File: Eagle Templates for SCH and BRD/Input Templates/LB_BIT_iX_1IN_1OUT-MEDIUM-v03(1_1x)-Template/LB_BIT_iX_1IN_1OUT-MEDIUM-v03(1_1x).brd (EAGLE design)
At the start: 21.4 x 18.2 mm, 17 parts, among them U1 LV321SOT23-5, U2 LV321SOT23-5

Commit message: added bitlab logo and made minor changes to board templates. Updated littlebits library.
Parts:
- added U$5: (no value), LITTLEBITS:BITLAB-LOGO
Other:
- board text added: "iX Name Here"
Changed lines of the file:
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@@
 <layer number="113" name="extra" color="10" fill="1" visible="yes" active="yes"/>
 <layer number="116" name="Patch_BOT" color="9" fill="4" visible="yes" active="yes"/>
+<layer number="118" name="Rect_Pads" color="7" fill="1" visible="no" active="yes"/>
 <layer number="121" name="_tsilk" color="7" fill="1" visible="yes" active="yes"/>
 <layer number="122" name="_bsilk" color="7" fill="1" visible="yes" active="yes"/>
@@
 <wire x1="3.305" y1="22.31" x2="2.51" y2="22.31" width="1" layer="46"/>
 <wire x1="2.51" y1="22.31" x2="2.51" y2="4.11" width="1" layer="46"/>
+<text x="21.6" y="13.21" size="1.3" layer="21" font="vector" rot="SR270" align="center">iX Name Here</text>
 </plain>
 <attributes>
@@
 <element name="U$1" library="LITTLEBITS" package="FABDWG01-OHW" value="FRAME-LETTER" x="0" y="0"/>
 <element name="U$4" library="ohw-logo" package="OSHW_FILLX150_NOTEXT" value="" x="19" y="16.9" rot="MR90"/>
+<element name="U$5" library="LITTLEBITS" package="BITLAB-LOGO" value="" x="19.5" y="15" rot="R270"/>
 </elements>
 <signals>

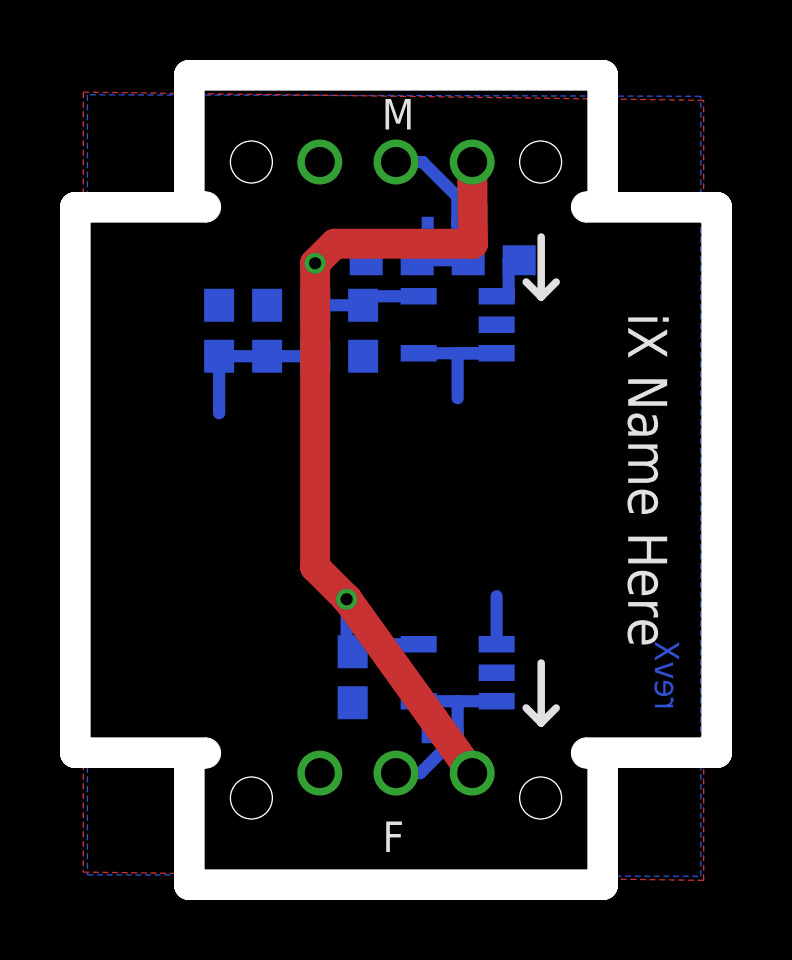
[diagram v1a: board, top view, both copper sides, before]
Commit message: Updated templates
- Added ferrite beads
- Moved text and annotations off of Nets layer
- Minor layout changes
- Removed I/O/W prefix from reference designators
- Removed output stage components from output bits
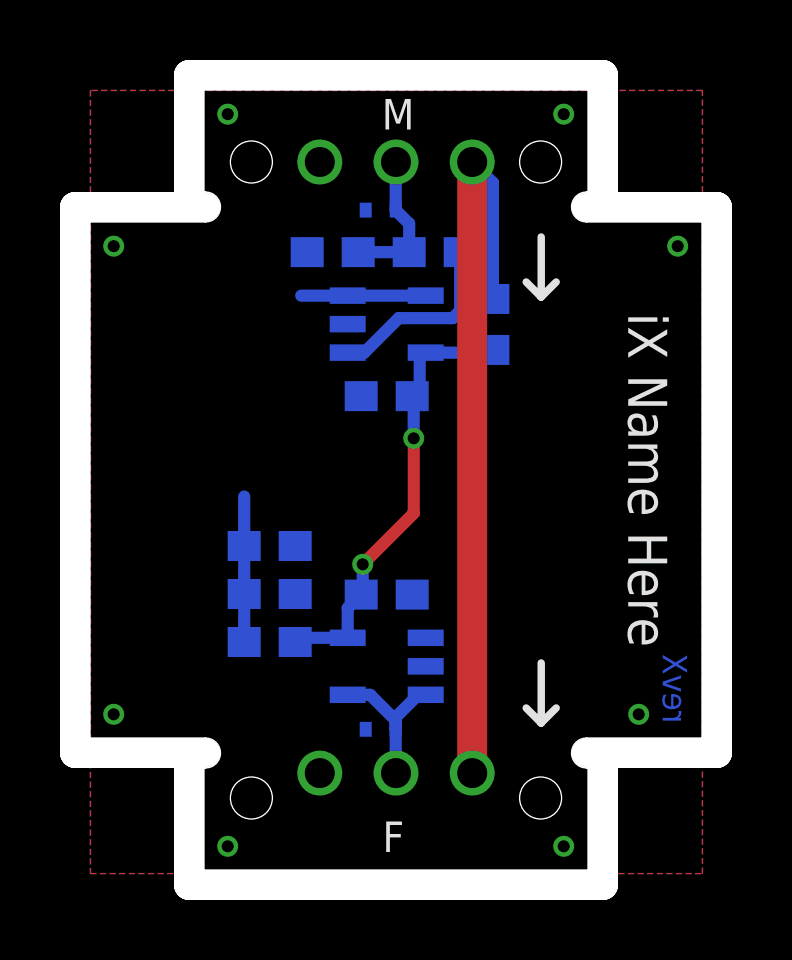
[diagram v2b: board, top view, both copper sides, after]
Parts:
- removed I?C1: 0.1uF, LITTLEBITS:CAP-0603
- removed I?C2: 10uF, LITTLEBITS:CAP-0603
- removed I?C3: 1.0uF, LITTLEBITS:CAP-0603
- removed I?R1: 1meg, LITTLEBITS:RES-0603
- removed I?R2: 10K, LITTLEBITS:RES-0603
- removed I?R3, I?R4: 3K3, LITTLEBITS:RES-0603
- removed I?TVS1, I?TVS2: ESD9B5.0ST5G, LITTLEBITS:SOD-923
- added C1: 0.1uF, LITTLEBITS:CAP-0603
- added C2: 10uF, LITTLEBITS:CAP-0603
- added C3: 1.0uF, LITTLEBITS:CAP-0603
- added FB1: FERRITE-BEAD0603, LITTLEBITS:R0603
- added R1: 1meg, LITTLEBITS:RES-0603
- added R2: 10K, LITTLEBITS:RES-0603
- added R3, R4: 3K3, LITTLEBITS:RES-0603
- added TVS1, TVS2: ESD9B5.0ST5G, LITTLEBITS:SOD-923
- U$1: value FRAME-LETTER -> OSHW-LOGOL; device LITTLEBITS:FABDWG01-OHW -> LITTLEBITS131206:OSHW-LOGO-L
- U$3: value OSHW-LOGOL -> FRAME-LETTER; device LITTLEBITS131206:OSHW-LOGO-L -> LITTLEBITS:FABDWG01-OHW
- moved U$1 77.8 mm to (-37.5, -68.2)
- moved U$3 76.5 mm to (0.00, 0.00)
- moved U$2 2.58 mm to (-92.2, -64.3)
- moved U2 2.37 mm to (12.9, 7.00)
- moved U1 2.37 mm to (12.9, 18.4), turned to 90 degrees
- renumbered I?BSF to BSF1, I?BSM to BSM1
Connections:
- new net LB_VCC: BSF1.VCC, BSM1.VCC1, FB1.2
- net GND: now also C1.2, C2.2, C3.1, R1.1, R4.1, TVS1.1, TVS2.1; no longer I?C1.2, I?C2.2, I?C3.1, I?R1.1, I?R4.1, I?TVS1.1, I?TVS2.1
- net N$4: now also R2.1; no longer I?R2.1
- net SIG_IN: now also R1.2, R2.2, TVS1.2; no longer I?R1.2, I?R2.2, I?TVS1.2
- net SIG_OUT: now also TVS2.2; no longer I?TVS2.2
- net VCC: now also C1.1, C3.2, FB1.1, R3.2; no longer BSF1.VCC, BSM1.VCC1, I?C1.1, I?C3.2, I?R3.2
- net VREF: now also C2.1, R3.1, R4.2; no longer I?C2.1, I?R3.1, I?R4.2
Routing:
- net LB_VCC: track 0.00 -> 25.2 mm
- net VCC: track 36.6 -> 15.4 mm
- net N$4: track 2.02 -> 6.28 mm
- net SIG_IN: track 6.70 -> 4.90 mm
- net N$3: track 1.60 -> 0.00 mm
- net N$2: track 5.40 -> 4.15 mm
- net SIG_OUT: track 6.32 -> 5.43 mm
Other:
- outline, holes or cut-outs redrawn
